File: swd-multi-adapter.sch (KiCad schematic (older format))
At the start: 5 parts, among them J1 SWD, J2 STDC14, J3 SWD, J4 JTAG, SW1 Reset

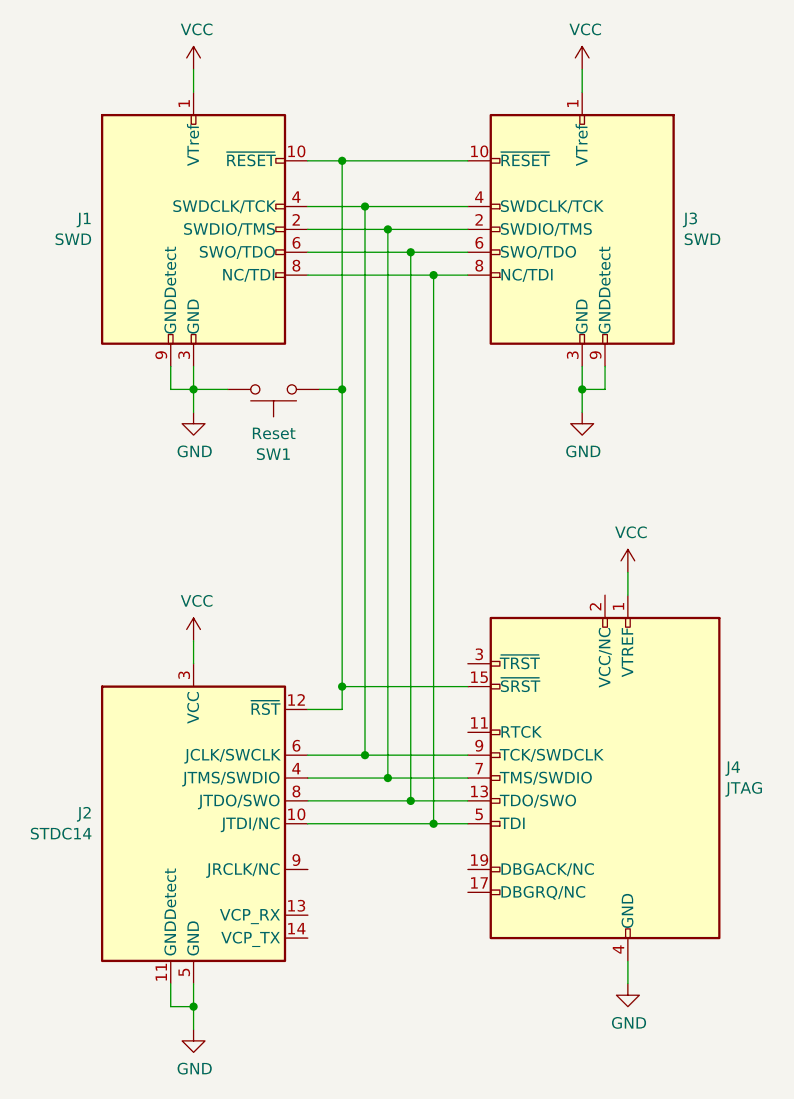
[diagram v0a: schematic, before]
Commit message: Added licensing info to the project files
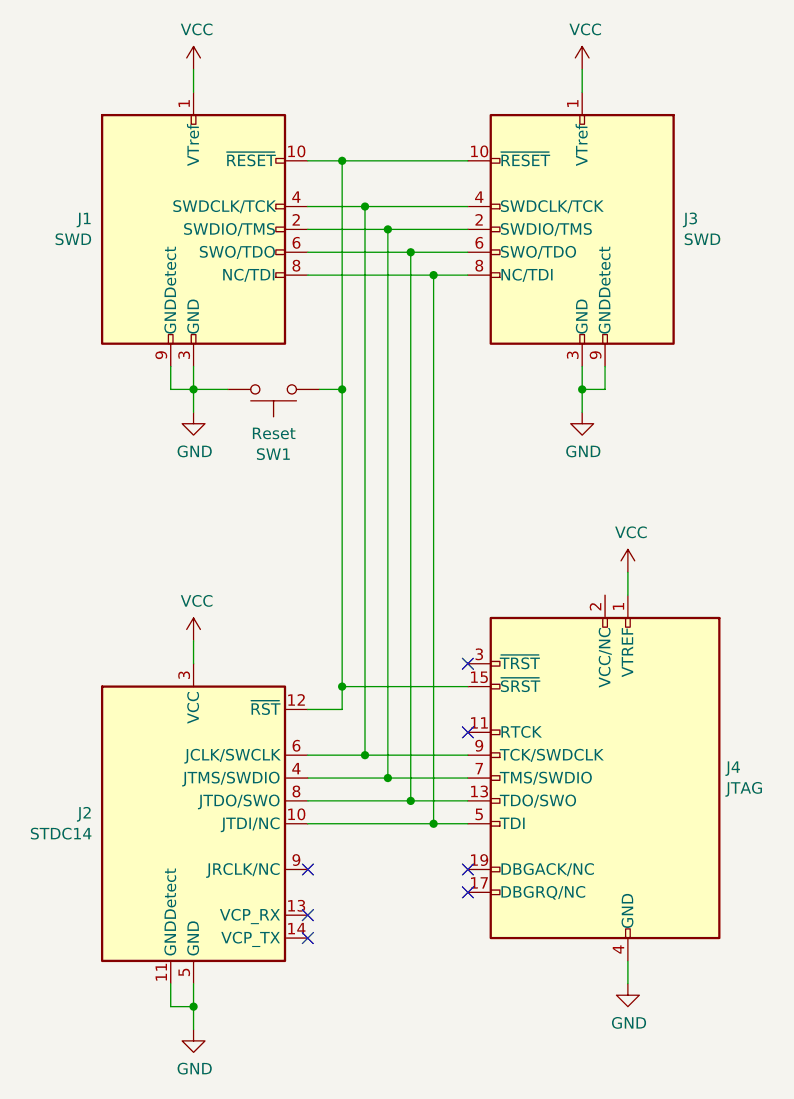
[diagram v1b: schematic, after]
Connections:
- no-connect marks 0 -> 7
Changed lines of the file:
@@
 Rev "1.0"
 Comp "Michal Potrzebicz"
-Comment1 ""
-Comment2 ""
-Comment3 ""
+Comment1 "https://creativecommons.org/licenses/by-sa/4.0/"
+Comment2 "Attribution-ShareAlike 4.0 International License"
+Comment3 "Released under the Creative Commons"
 Comment4 ""
 $EndDescr
@@
 Wire Wire Line
 	4850 2700 4850 1700
+NoConn ~ 4700 4800
+NoConn ~ 4700 5000
+NoConn ~ 4700 5100
+NoConn ~ 5400 4800
+NoConn ~ 5400 4900
+NoConn ~ 5400 4200
+NoConn ~ 5400 3900
 $EndSCHEMATC
